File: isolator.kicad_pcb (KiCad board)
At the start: 4 copper layers, 120 x 75 mm, 125 parts, among them J1 HOST, J2 USB_C_Receptacle_PowerOnly_6P, J3 USB_A, J4 USB_A, J5 USB_C_Receptacle_USB2.0_16P, J6 USB_C_Receptacle_USB2.0_16P, Q1 2N7002, Q2 2N7002, T1 750313638, U1 ADuM4165, U10 TPS2553DBV, U11 TPS2553DBV, U12 TPS2553DBV, U13 TLV7041DBV, U14 TLV7041DBV, U15 USBLC6-2SC6, U16 USBLC6-2SC6, U17 USBLC6-2SC6, U18 USBLC6-2SC6, U2 USBLC6-2SC6, U3 USBLC6-2SC6, U4 USB2514B_Bi, U5 SN6505BDBV, U6 MIC29302WU, U7 TPS2121, U8 AP2112K-3.3, U9 TPS2553DBV, Y1 24M 8pF, Y2 24M 12pF

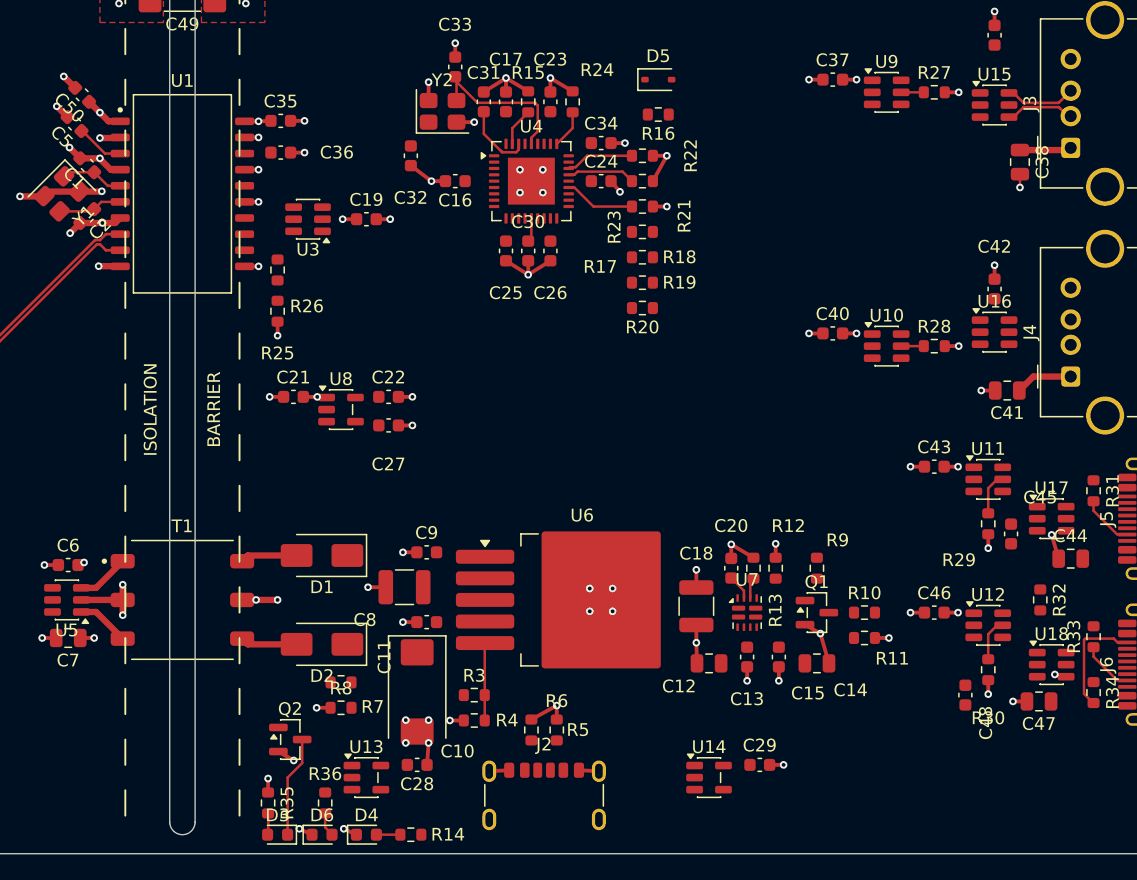
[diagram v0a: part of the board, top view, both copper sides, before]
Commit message: style(pcb): 45/90 tidy pass
All 23 track segments whose angle was not a multiple of 45 degrees have been
replaced by two-segment doglegs with identical endpoints, width, layer and net.
For each one both dogleg orientations (axis-first and 45-first) were built and
clearance-checked against an exact obstacle model; the orientation whose corner
sits furthest from other copper was kept.

The 23 were 20 GND2 plane-stitching stubs, one /VBUS_HOST stub, one /ISO_5V
stub and one 0.129 mm GND1 jog at U1.  None needed to be left as-is.

Removal of the originals was done in a separate pcbnew session after the
replacements were added, then the zones were refilled.

Verified: 0 segments off the 45/90 grid remain.
DRC unchanged (102 violations, 170 unconnected), shorting 0, dangling 0.

Co-Authored-By: Claude Fable 5 <noreply@anthropic.com>
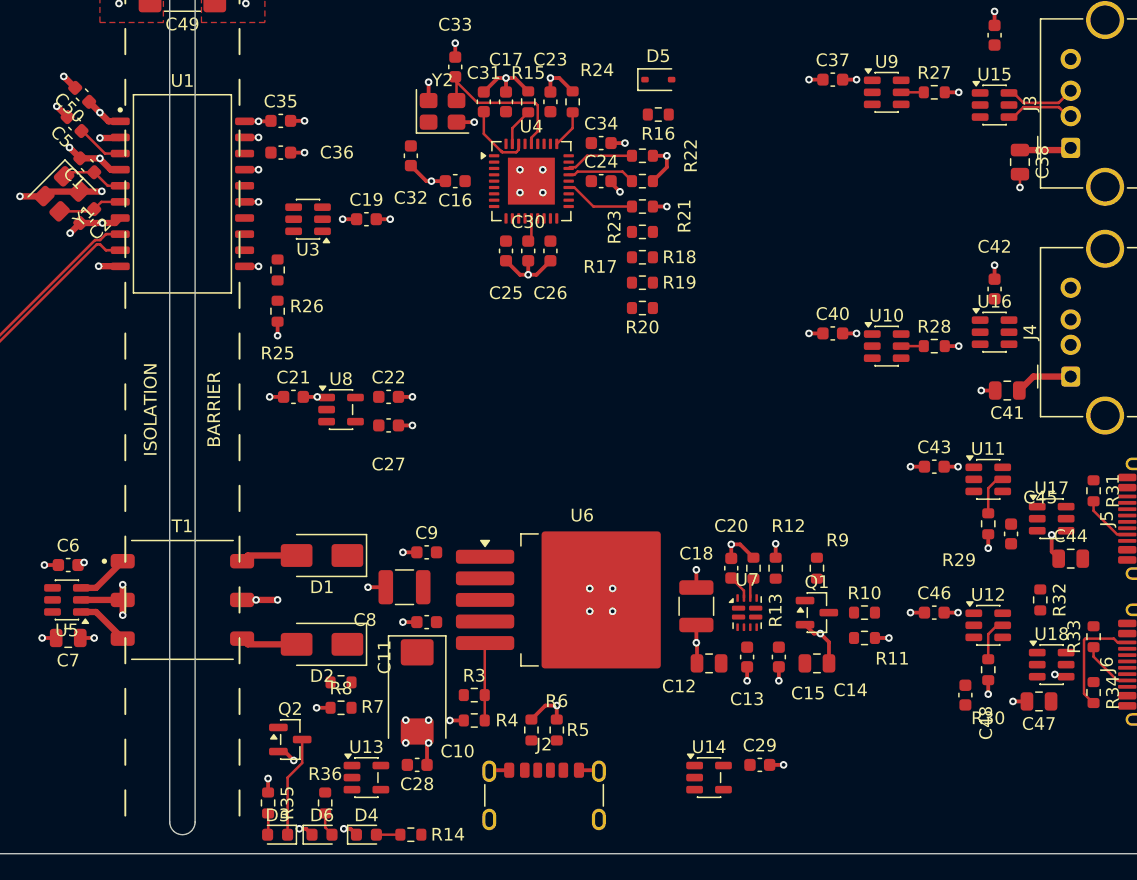
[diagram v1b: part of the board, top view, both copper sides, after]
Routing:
- net GND2: track 91.6 -> 93.8 mm

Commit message: feat: swap hub port bundles 1<->4 2<->3 for crossing-free fanout (sch+pcb)
U4 (USB2514B) is at rot 0 with all four downstream port pin bundles on its
WEST edge, while all four ports are on the far EAST side and are approached
heading east.  Any path from "heading west" to "heading east" is a 180 degree
turn, which reverses the transverse order of the ribbon: the pairs left U4 as
P1,P2,P3,P4 (north->south) and arrived as P4,P3,P2,P1, while the destinations
need P1,P2,P3,P4.  That is a full reversal of four items = 6 pair-to-pair
crossings, i.e. at least three crossunders (12 vias) on 480 Mbit/s pairs.
No rotation of U4 fixes it - handedness is preserved under rotation.

Hub ports 1-4 are functionally identical, so the fix is a net swap, not copper.
Full bundles move together (data pair + PRTPWR/BC_EN + OCS_N) so each port's
power switch and fault line stay with their own data pair:

  hub port1 <- port4   hub port2 <- port3
  hub port3 <- port2   hub port4 <- port1

Schematic: the 16 net labels on U4's downstream pin column (x = 463.55) were
renamed.  Nothing else moved - connector-side nets, TPS2553 switches, ILIM
resistors, ESD parts and VBUS are untouched.

PCB: the 16 affected U4 pads were re-netted in a mutation-only session, each
one cross-checked against a fresh `kicad-cli sch export netlist` before saving;
all 37 U4 pads verified to match the netlist afterwards.

Verification
  ERC severity-error: 0 violations, exit 0
  /PnD+- now = {U4 <new pin>, USBLC6 x2, connector}
    P1 -> U4 pins 8/9 (was 1/2)   P2 -> pins 6/7   P3 -> pins 3/4   P4 -> 1/2
  /PRTPWRn = exactly {U4 pin, TPS2553 pin 3} for all four
  /nOCSn   = {U4 pin, TPS2553 pin 4, pull-up} for all four
  GND1 n GND2 = {U1, C49} unchanged
  DRC unchanged: 102 violations, 170 unconnected, shorting 0, dangling 0

Co-Authored-By: Claude Fable 5 <noreply@anthropic.com>
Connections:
- U4 pad 1: /P1_D- -> /P4_D-
- U4 pad 12: /PRTPWR1 -> /PRTPWR4
- U4 pad 13: /nOCS1 -> /nOCS4
- U4 pad 16: /PRTPWR2 -> /PRTPWR3
- U4 pad 17: /nOCS2 -> /nOCS3
- U4 pad 18: /PRTPWR3 -> /PRTPWR2
- U4 pad 19: /nOCS3 -> /nOCS2
- U4 pad 2: /P1_D+ -> /P4_D+
- U4 pad 20: /PRTPWR4 -> /PRTPWR1
- U4 pad 21: /nOCS4 -> /nOCS1
- U4 pad 3: /P2_D- -> /P3_D-
- U4 pad 4: /P2_D+ -> /P3_D+
- U4 pad 6: /P3_D- -> /P2_D-
- U4 pad 7: /P3_D+ -> /P2_D+
- U4 pad 8: /P4_D- -> /P1_D-
- U4 pad 9: /P4_D+ -> /P1_D+
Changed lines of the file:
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@@
 			(layers "F.Cu" "F.Mask" "F.Paste")
 			(roundrect_rratio 0.25)
-			(net "/P1_D-")
+			(net "/P4_D-")
 			(pinfunction "USBDM_DN1/PRT_DIS_M1_1")
 			(pintype "bidirectional")
@@
 			(layers "F.Cu" "F.Mask" "F.Paste")
 			(roundrect_rratio 0.25)
-			(net "/P1_D+")
+			(net "/P4_D+")
 			(pinfunction "USBDP_DN1/PRT_DIS_P1_2")
 			(pintype "bidirectional")
@@
 			(layers "F.Cu" "F.Mask" "F.Paste")
 			(roundrect_rratio 0.25)
-			(net "/P2_D-")
+			(net "/P3_D-")
 			(pinfunction "USBDM_DN2/PRT_DIS_M2_3")
 			(pintype "bidirectional")
@@
 			(layers "F.Cu" "F.Mask" "F.Paste")
 			(roundrect_rratio 0.25)
-			(net "/P2_D+")
+			(net "/P3_D+")
 			(pinfunction "USBDP_DN2/PRT_DIS_P2_4")
 			(pintype "bidirectional")
@@
 			(layers "F.Cu" "F.Mask" "F.Paste")
 			(roundrect_rratio 0.25)
-			(net "/P3_D-")
+			(net "/P2_D-")
 			(pinfunction "USBDM_DN3/PRT_DIS_M3_6")
 			(pintype "bidirectional")
@@
 			(layers "F.Cu" "F.Mask" "F.Paste")
 			(roundrect_rratio 0.25)
-			(net "/P3_D+")
+			(net "/P2_D+")
 			(pinfunction "USBDP_DN3/PRT_DIS_P3_7")
 			(pintype "bidirectional")
@@
 			(layers "F.Cu" "F.Mask" "F.Paste")
 			(roundrect_rratio 0.25)
-			(net "/P4_D-")
+			(net "/P1_D-")
 			(pinfunction "USBDM_DN4/PRT_DIS_M4_8")
 			(pintype "bidirectional")
@@
 			(layers "F.Cu" "F.Mask" "F.Paste")
 			(roundrect_rratio 0.25)
-			(net "/P4_D+")
+			(net "/P1_D+")
 			(pinfunction "USBDP_DN4/PRT_DIS_P4_9")
 			(pintype "bidirectional")
@@
 			(layers "F.Cu" "F.Mask" "F.Paste")
 			(roundrect_rratio 0.25)
-			(net "/PRTPWR1")
+			(net "/PRTPWR4")
 			(pinfunction "PRTPWR1/BC_EN1_12")
 			(pintype "bidirectional")
@@
 			(layers "F.Cu" "F.Mask" "F.Paste")
 			(roundrect_rratio 0.25)
-			(net "/nOCS1")
+			(net "/nOCS4")
 			(pinfunction "OCS_N1_13")
 			(pintype "input")
@@
 			(layers "F.Cu" "F.Mask" "F.Paste")
 			(roundrect_rratio 0.25)
-			(net "/PRTPWR2")
+			(net "/PRTPWR3")
 			(pinfunction "PRTPWR2/BC_EN2_16")
 			(pintype "bidirectional")
@@
 			(layers "F.Cu" "F.Mask" "F.Paste")
 			(roundrect_rratio 0.25)
-			(net "/nOCS2")
+			(net "/nOCS3")
 			(pinfunction "OCS_N2_17")
 			(pintype "input")
@@
 			(layers "F.Cu" "F.Mask" "F.Paste")
 			(roundrect_rratio 0.25)
-			(net "/PRTPWR3")
+			(net "/PRTPWR2")
 			(pinfunction "PRTPWR3/BC_EN3_18")
 			(pintype "bidirectional")
@@
 			(layers "F.Cu" "F.Mask" "F.Paste")
 			(roundrect_rratio 0.25)
-			(net "/nOCS3")
+			(net "/nOCS2")
 			(pinfunction "OCS_N3_19")
 			(pintype "input")
@@
 			(layers "F.Cu" "F.Mask" "F.Paste")
 			(roundrect_rratio 0.25)
-			(net "/PRTPWR4")
+			(net "/PRTPWR1")
 			(pinfunction "PRTPWR4/BC_EN4_20")
 			(pintype "bidirectional")
@@
 			(layers "F.Cu" "F.Mask" "F.Paste")
 			(roundrect_rratio 0.25)
-			(net "/nOCS4")
+			(net "/nOCS1")
 			(pinfunction "OCS_N4_21")
 			(pintype "input")

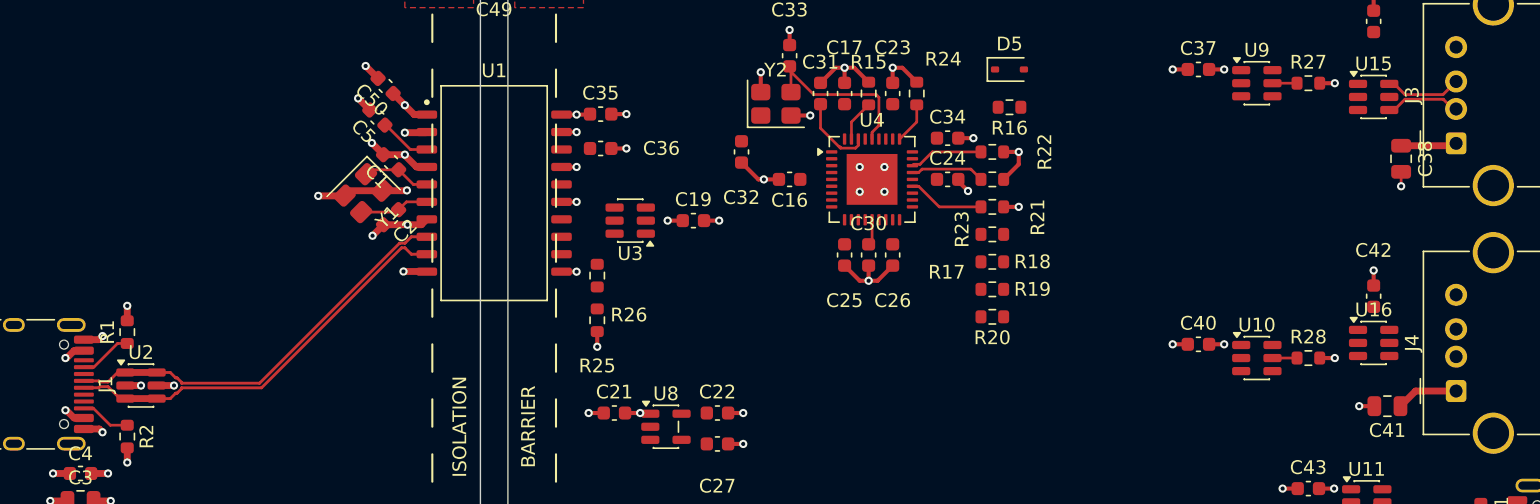
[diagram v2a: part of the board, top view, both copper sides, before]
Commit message: feat(pcb): route USB differential pairs + A/B-row ties
Lands the differential-pair copper that the previous pass designed but could
not emit.  All members 0.21 mm, 0.337 mm centre-to-centre, 45/90 only, coupled
bends, F.Cu except the ISO long haul.

Landed
  ISO_D  U1 -> U3  (F.Cu)            skew -0.008 mm
  ISO_D  U3 -> U4  (B.Cu + 4 vias)   skew +0.680 mm
  P1_D   U4 -> U15 (F.Cu)            skew +1.168 mm
  P2_D   U4 -> U16 (F.Cu)            skew +1.085 mm
  P2_D   U16 -> J4 (F.Cu)            skew  0.000 mm
  HOST_D J1 B6/B7 -> U2  A/B-row ties, spliced onto the owner's existing
         0.5 mm U2 escapes (extended, nothing ripped)

Enabling change: /HUB_XO ran straight up U4 pad 31's own column (x=116.5) to
reach pad 32, leaving the ISO pair no way into pads 30/31 - the C17/R15/C23 row
offers exactly one vertical channel there.  Three of its segments are replaced
by a route that leaves that channel at y=65.2 and crosses to pad 32's own
column below the ISO via row.

Not landed: P3/P4 long hauls and the U17->J5 / U18->J6 legs; see
scratchpad/pcb/routing-pass-report.md for the bottleneck analysis.

DRC: 102 violations (unchanged type-for-type vs baseline), shorting 0,
track_dangling 0, via_dangling 5, unconnected 170 -> 158.

Co-Authored-By: Claude Fable 5 <noreply@anthropic.com>
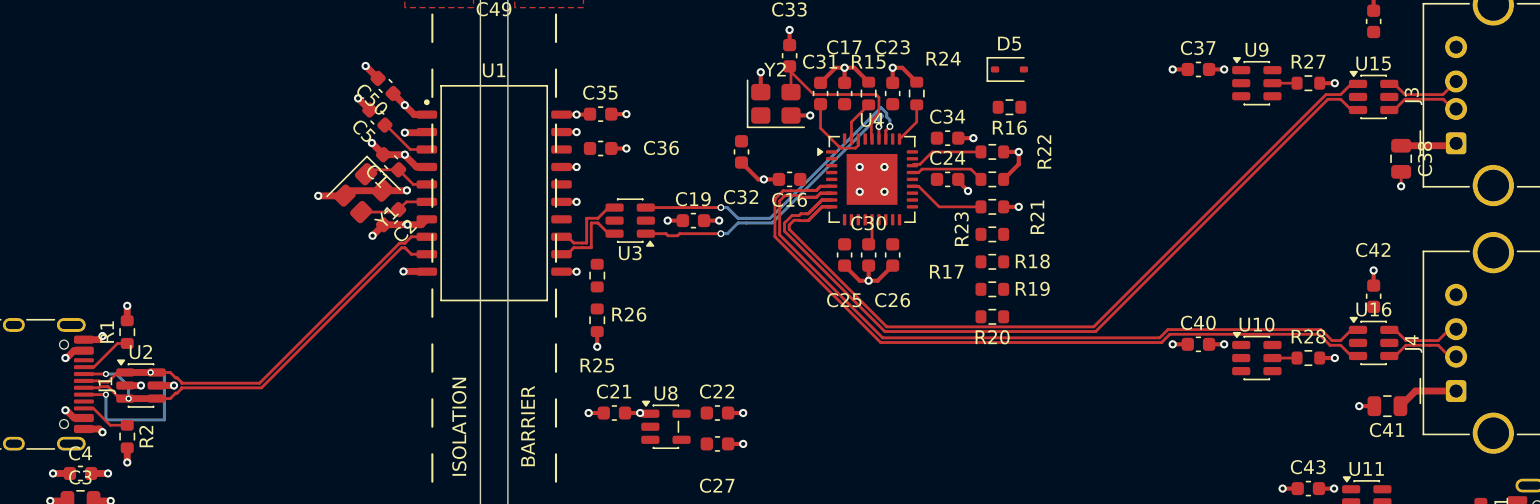
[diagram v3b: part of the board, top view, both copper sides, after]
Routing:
- net /P2_D-: track 0.00 -> 61.3 mm
- net /P2_D+: track 0.00 -> 60.2 mm
- net /P1_D-: track 5.48 -> 64.6 mm
- net /P1_D+: track 5.58 -> 63.5 mm
- net /ISO_D-: track 0.00 -> 29.6 mm, vias 0 -> 2
- net /ISO_D+: track 0.00 -> 29.0 mm, vias 0 -> 2
- net /HOST_D+: track 30.0 -> 42.2 mm, vias 0 -> 2
- net /HOST_D-: track 30.1 -> 34.6 mm, vias 0 -> 2

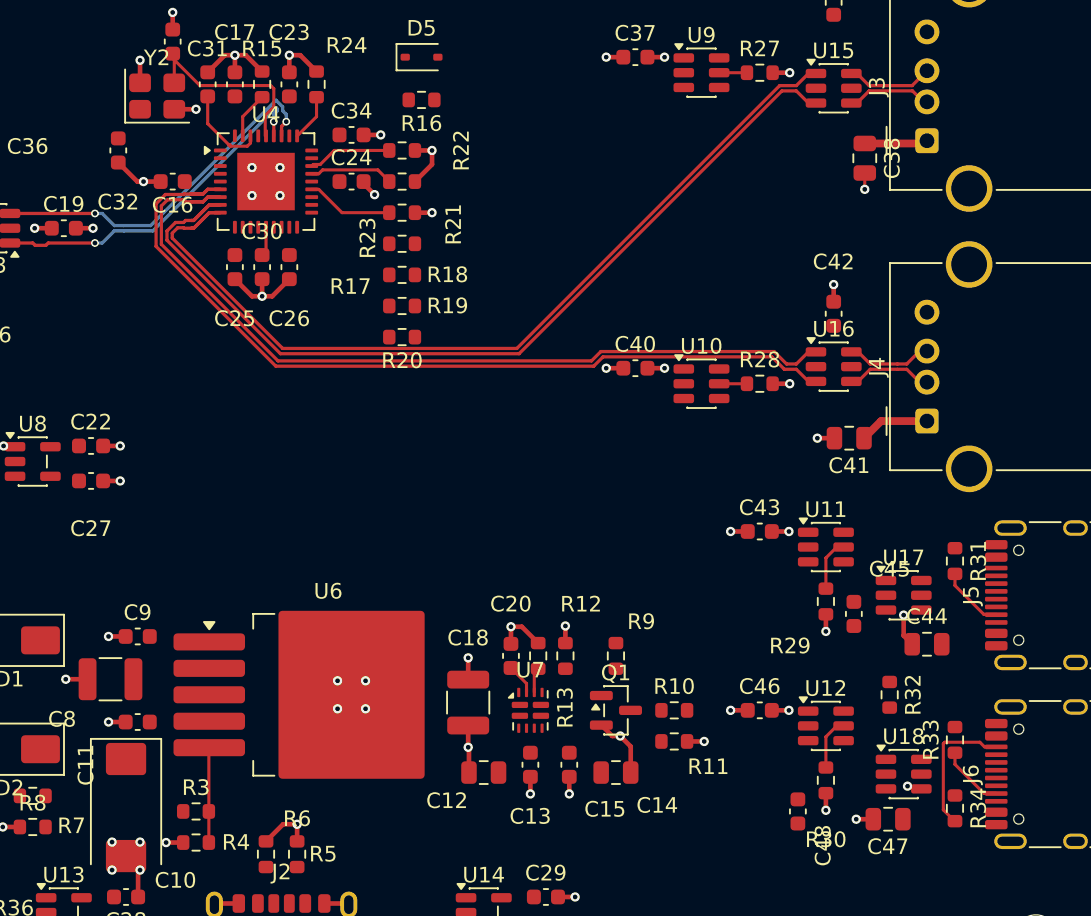
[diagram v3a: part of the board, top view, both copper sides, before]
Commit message: feat(pcb): complete USB pair routing — P3/P4 B.Cu detour, J5/J6 ties, CC crossunders
All six differential pairs are now routed end to end.

* ISO_D U3->U4 re-run north on B.Cu (its old diagonal sat exactly where P3/P4
  need to dive).  Old B.Cu removed in its own session, re-added after.
* P3/P4 escape U4 on F.Cu, dive to B.Cu in the 0.55 mm slot between the ISO
  haul and the GND2 stitch via at (108.125, 70), descend past the C16/C32
  pinch, and surface south of P1/P2's east runs.  2 vias per member,
  16-19 mm of B.Cu each, entirely inside the x>93.5 In2 pour.
* P3 needs a second 4 mm B.Cu hop to reach U17: R29 and C45 leave only a
  0.10 mm wide F.Cu window at y=96.6, so the pair passes under them and
  surfaces in the 0.95 mm slot at x=154.7.
* J5/J6 A/B-row ties landed (one crossunder each, 0.45/0.25).
* /P3_CC1, /P4_CC1, /P4_CC2 ripped and re-routed with a B.Cu crossunder each
  (0.15 mm track, 0.45/0.25 vias - the only way two independent crossunders
  fit the 1.32 mm pocket between R33/R34's pads and the J6 tie).
* +0.28 mm length-match bump on P4_D+ and +0.124 mm on ISO_D+ (both single
  45 deg jogs, not serpentines).

The U4 fan-out was rebuilt as a common 45 deg translate followed by a
symmetric +-0.15 mm pitch jog, so the 0.5 -> 0.8 mm via-pitch change costs no
skew.  A hole-to-copper (0.254 mm) check was added to the offline validator
after DRC caught two violations it could not see.

DRC: 102 violations, no new types vs baseline; shorting 0, track_dangling 0,
via_dangling 5; unconnected 170 -> 146.

Co-Authored-By: Claude Fable 5 <noreply@anthropic.com>
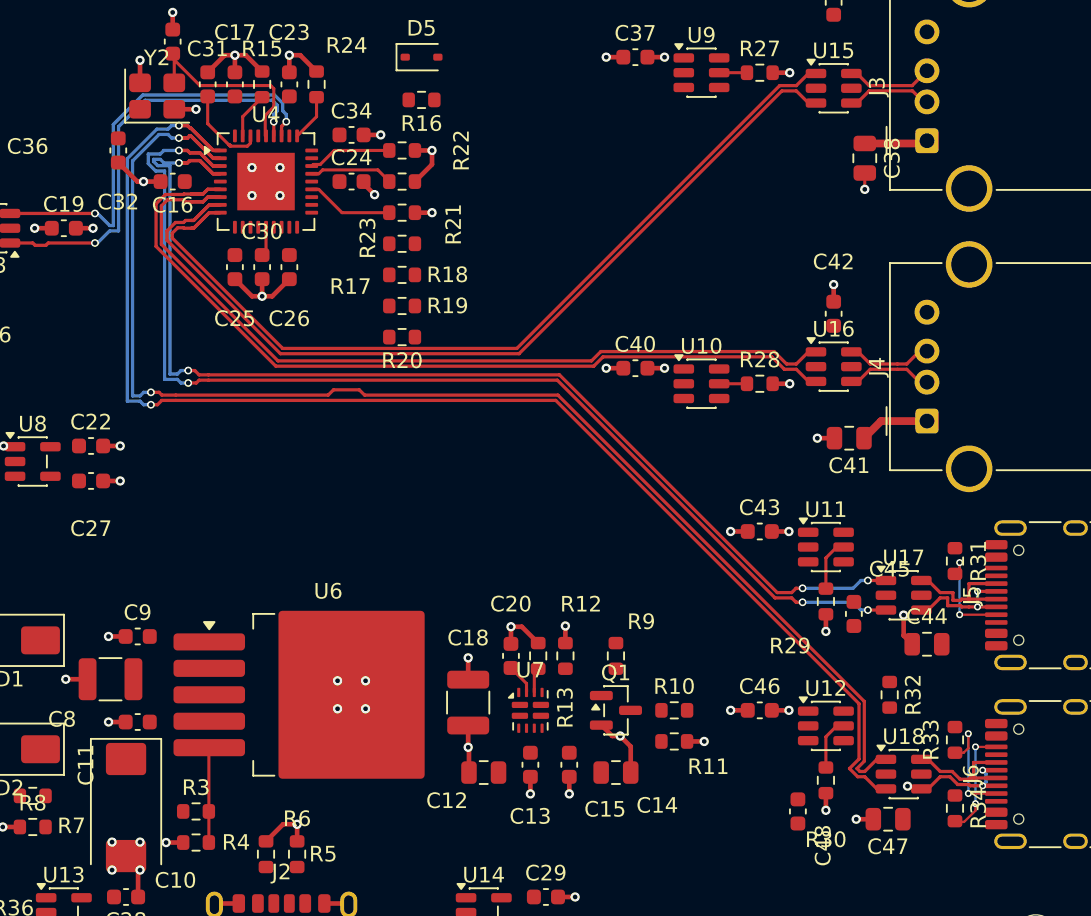
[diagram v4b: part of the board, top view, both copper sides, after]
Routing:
- net /P4_D-: track 0.00 -> 96.5 mm, vias 1 -> 5
- net /P4_D+: track 0.00 -> 95.8 mm, vias 0 -> 2
- net /P3_D-: track 0.00 -> 84.0 mm, vias 0 -> 6
- net /P3_D+: track 0.00 -> 83.4 mm, vias 0 -> 4
- net /ISO_D+: track 29.0 -> 33.4 mm
- net /ISO_D-: track 29.6 -> 33.9 mm
- net /P4_CC1: track 4.17 -> 7.55 mm, vias 0 -> 2
- net /P3_CC1: track 4.17 -> 6.55 mm, vias 0 -> 2
- net /P4_CC2: track 8.88 -> 7.05 mm, vias 0 -> 2
